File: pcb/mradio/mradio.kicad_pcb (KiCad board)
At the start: 6 copper layers, 132.2 x 75 mm, 191 parts, among them J101 Conn_02x07_Odd_Even, J202 Conn_01x02, J301 2250065-1, J401 MM60-52B1-E1-R650, J501 MDT420E01001, Q101 Q_NMOS, Q102 Q_NMOS, Q103 Q_NMOS, Q104 Q_NMOS, Q105 Q_NMOS, Q106 Q_NMOS, Q107 Q_NMOS, Q108 Q_NMOS, Q301 SSM3K56FS_LF, U1 STM32H745ZITx, U301 DP83825I, U401 74AVC4T774, U402 74AVC4T774, U502 SN74LVC1T45DRL, U601 TPS54560BDDA, U701 TPS54560BDDA, U801 TPS7A8500ARGRR, U901 TPS7A8500ARGRR, Y301 DSC1525JL2A-25M00000T

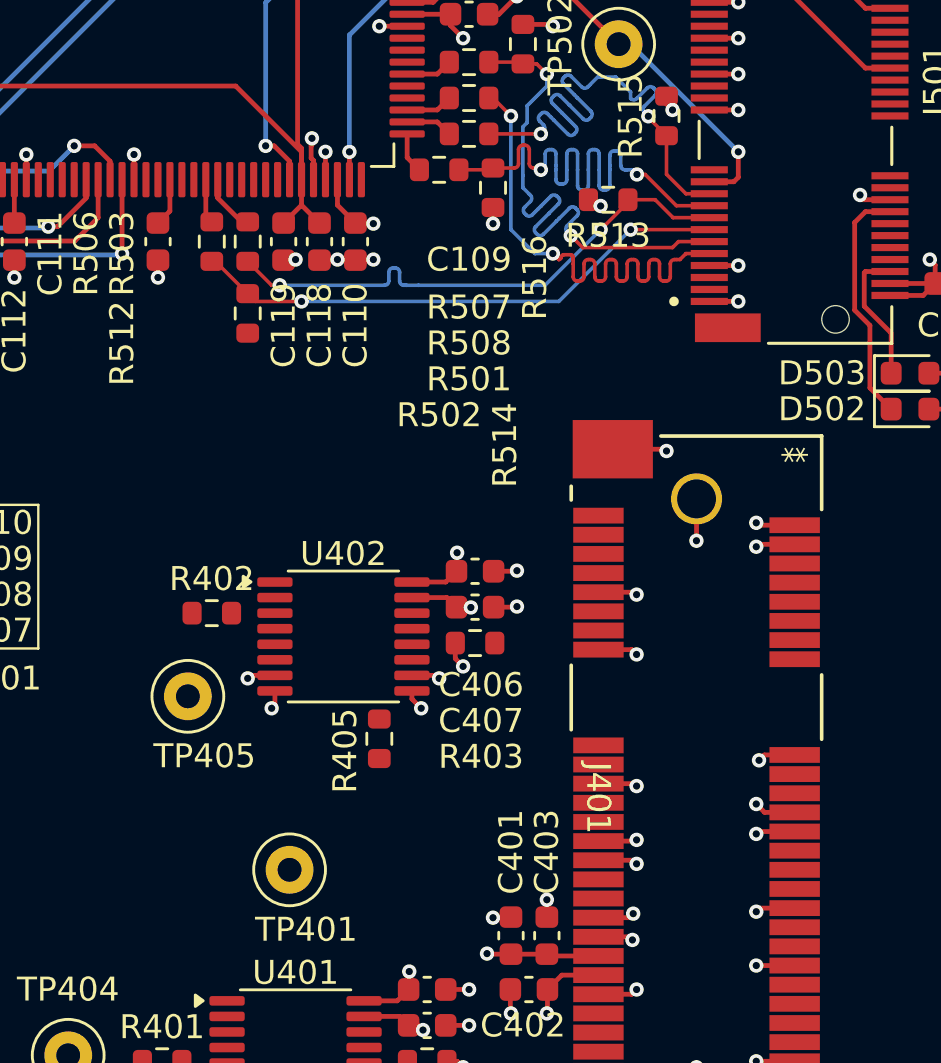
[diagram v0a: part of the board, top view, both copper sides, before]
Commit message: add some more 900 MHz traces
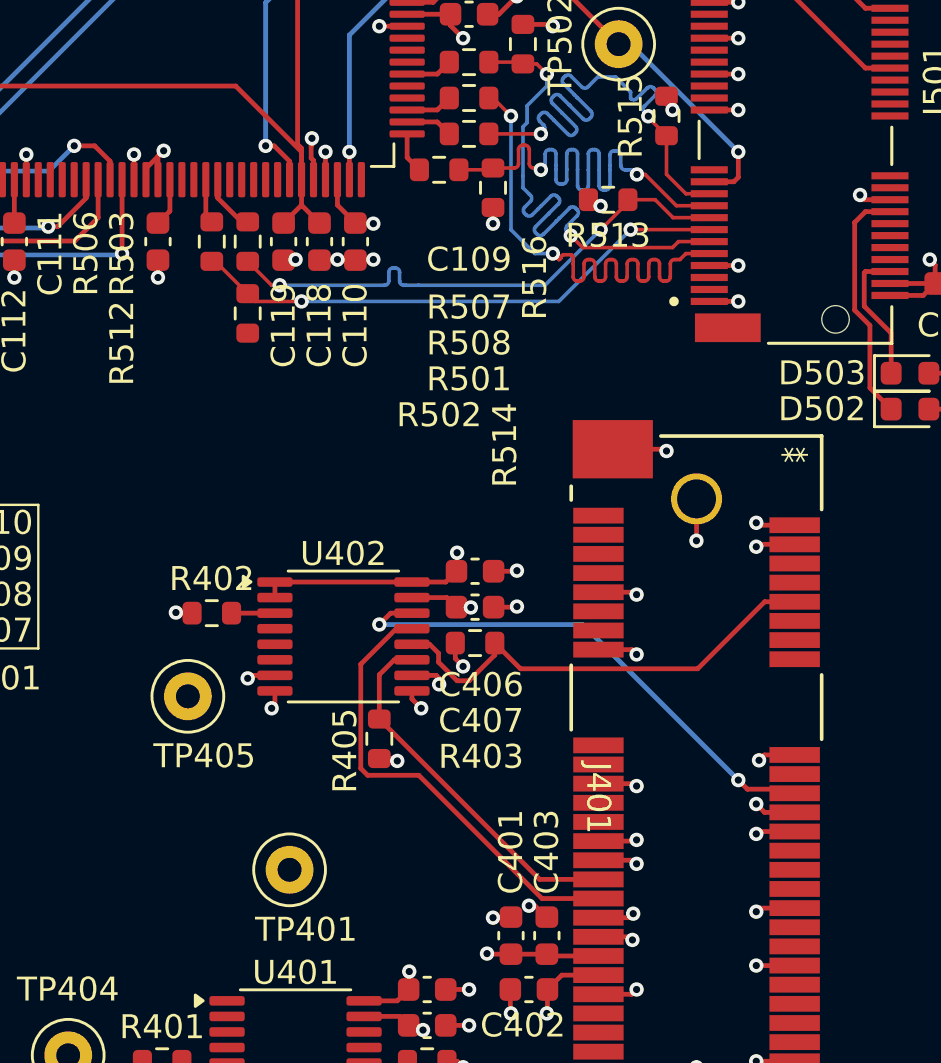
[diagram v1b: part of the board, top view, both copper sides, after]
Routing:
- net /900 Mhz/WM_RESET_3V3: track 0.00 -> 21.8 mm, vias 0 -> 2
- net /900 Mhz/SPI_INT_3V3: track 0.00 -> 19.4 mm
- net /900 Mhz/WM_WAKE_3V3: track 0.00 -> 19.3 mm
- net /900 Mhz/WM_BUSY_3V3: track 0.00 -> 15.4 mm
- net +1V8: track 64.1 -> 71.2 mm, vias 26 -> 27
- net +3V3: track 41.7 -> 44.5 mm, vias 23 -> 24
- net WM_RESET: track 0.00 -> 1.81 mm
- net GND: track 117.4 -> 118.6 mm, vias 99 -> 100

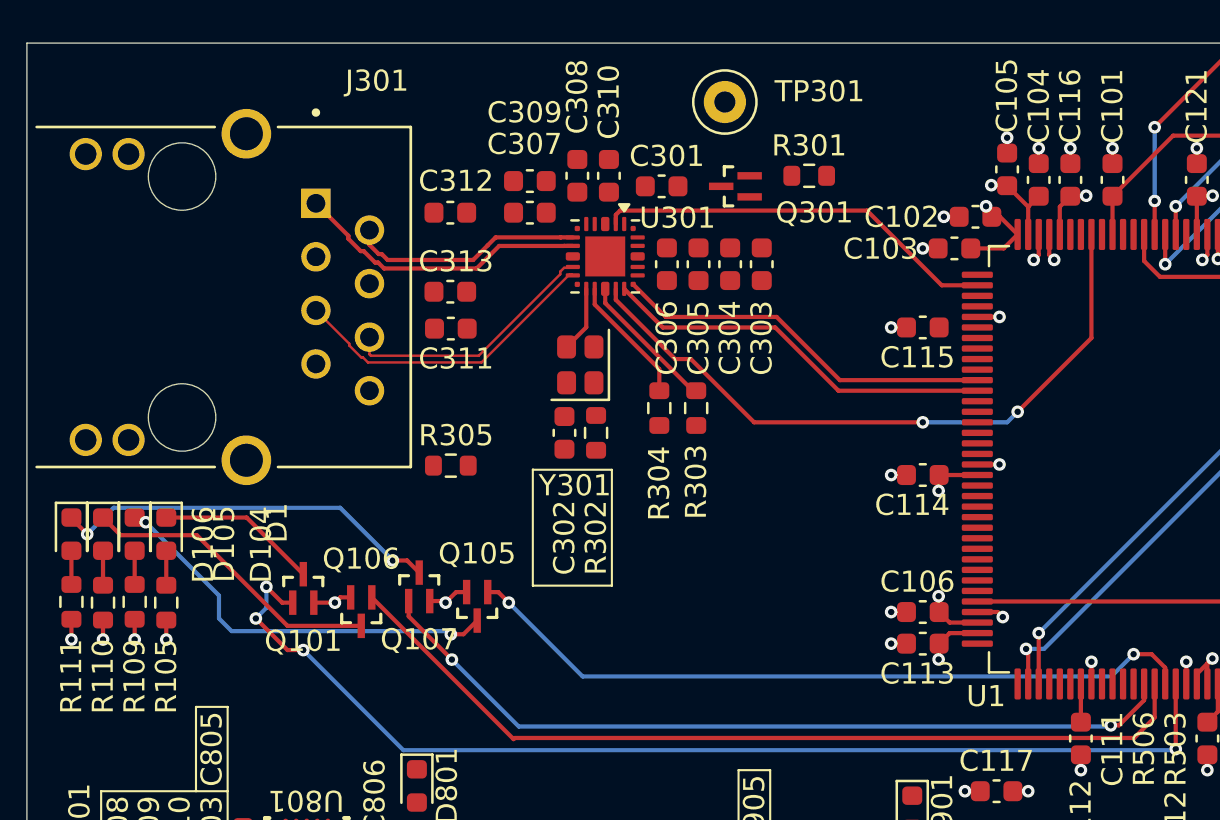
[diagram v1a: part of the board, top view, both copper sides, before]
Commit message: eth routing
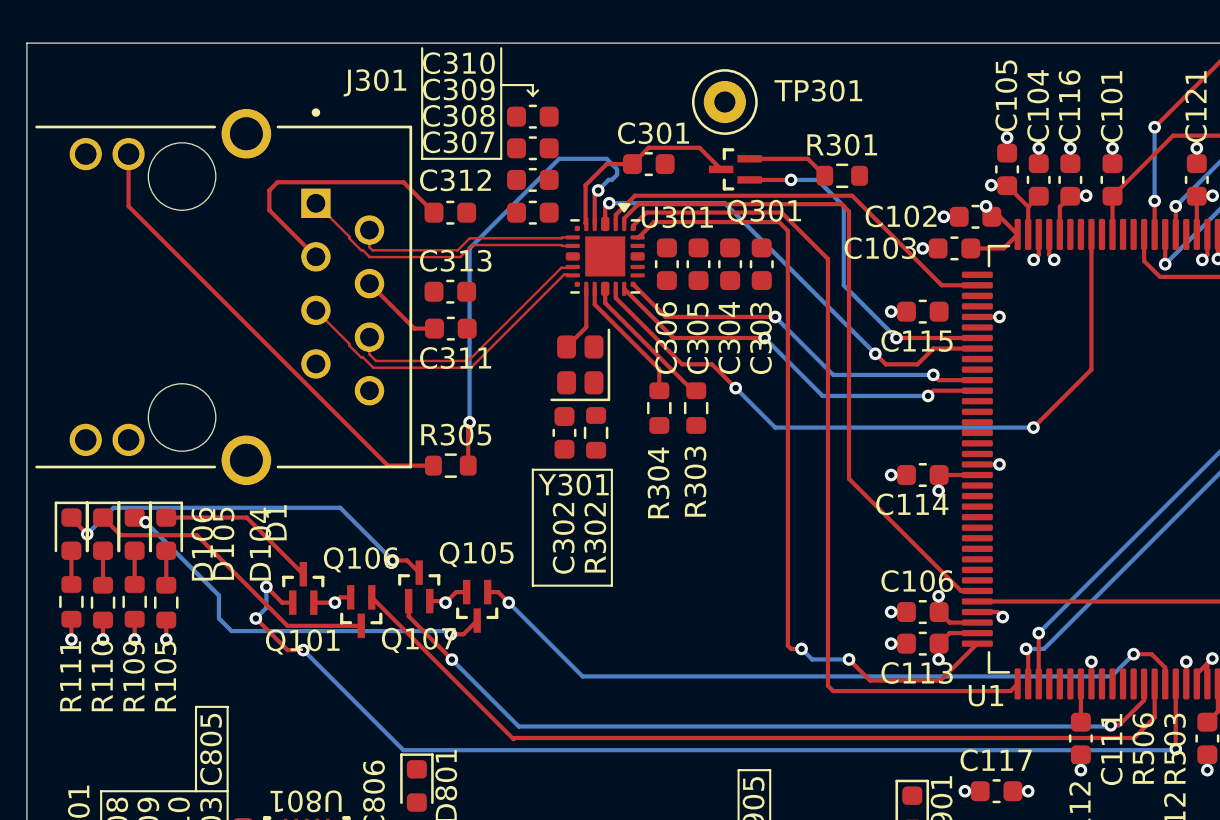
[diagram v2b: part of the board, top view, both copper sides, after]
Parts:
- moved C310 4.57 mm to (79.2, 56.0), turned to 0 degrees
- moved C308 2.12 mm to (79.2, 59.0), turned to 0 degrees
- moved R301 1.56 mm to (93.9, 58.8)
- moved C309 1.56 mm to (79.2, 57.5)
- moved C301 1.22 mm to (84.8, 58.2)
- moved Q301 0.80 mm to (88.9, 58.5)
- moved C115 0.75 mm to (97.8, 65.2)
- moved C307 0.14 mm to (79.2, 60.6)
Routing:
- net ETH_TXD1: track 0.00 -> 40.0 mm
- net ETH_TXD0: track 0.00 -> 37.7 mm, vias 0 -> 2
- net ETH_TX_EN: track 0.00 -> 32.3 mm
- net /Ethernet/ETH_LINK: track 0.00 -> 23.0 mm, vias 0 -> 2
- net ETH_INT: track 0.00 -> 22.2 mm, vias 0 -> 2
- net Net-(J301-Pad9): track 0.00 -> 22.0 mm
- net ETH_RESET: track 0.00 -> 16.1 mm, vias 0 -> 2
- net Net-(J301-RCT): track 0.00 -> 12.6 mm
- net Net-(Q301-D): track 0.00 -> 9.45 mm
- net Net-(J301-TCT): track 0.00 -> 3.97 mm
- net Net-(Q301-S): track 0.00 -> 3.90 mm
- net ETH_MDC: track 32.1 -> 33.1 mm
- net /Ethernet/ETH_RD-: track 11.6 -> 10.8 mm
- net ETH_REF_CLK: track 19.1 -> 19.7 mm
- net ETH_RXD1: track 18.8 -> 19.0 mm, vias 0 -> 2
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
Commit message: eth changes
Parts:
- moved C303 2.44 mm to (92.5, 62.5)
- moved C304 2.44 mm to (91.0, 62.5)
- moved C305 2.44 mm to (89.5, 62.5)
- moved C306 1.34 mm to (86.5, 64.0), turned to 180 degrees
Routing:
- net ETH_TXD1: track 40.0 -> 0.00 mm
- net ETH_TXD0: track 37.7 -> 0.05 mm, vias 2 -> 0
- net ETH_TX_EN: track 32.3 -> 0.00 mm
- net ETH_CRS_DV: track 0.00 -> 18.1 mm
- net +1V8: track 71.2 -> 72.9 mm
- net ETH_RXD1: track 19.0 -> 18.8 mm, vias 2 -> 0
- net ETH_RXD0: vias 2 -> 0

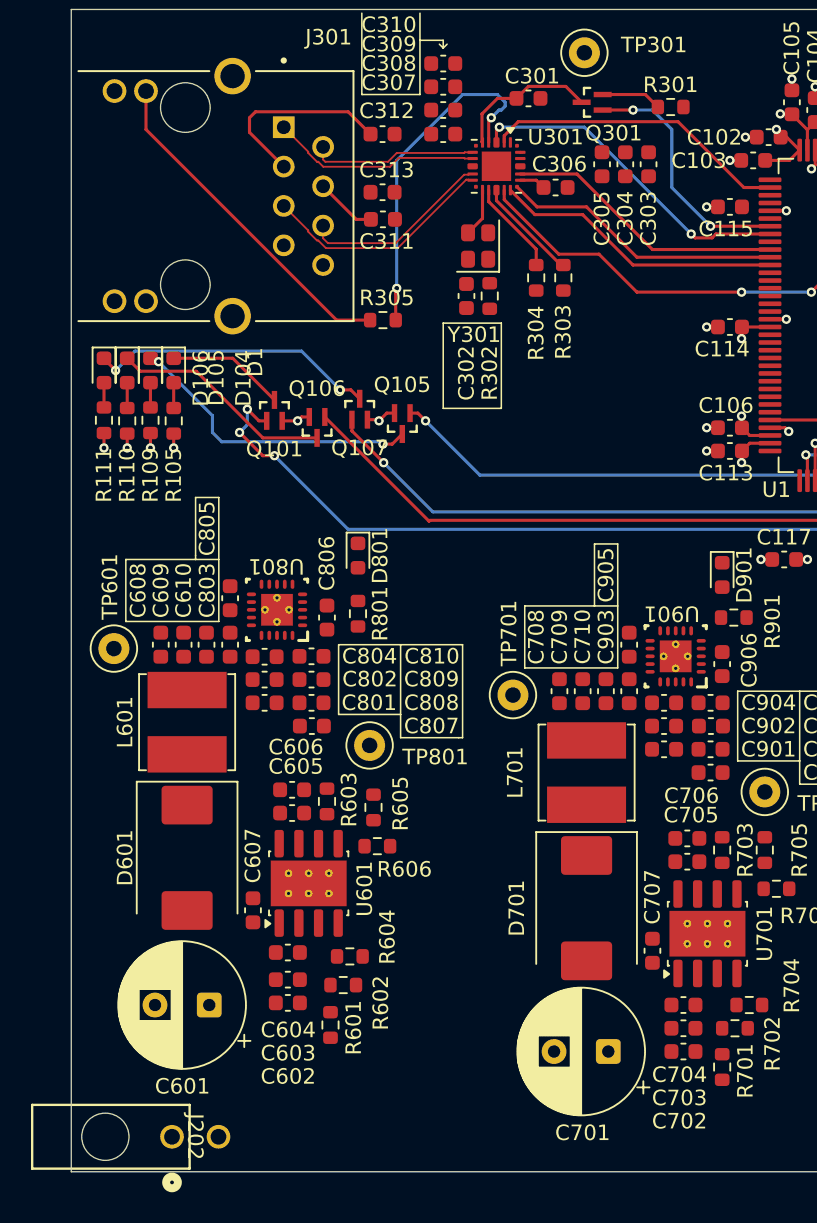
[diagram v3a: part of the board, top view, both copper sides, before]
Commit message: 12v to 3v3 circuit
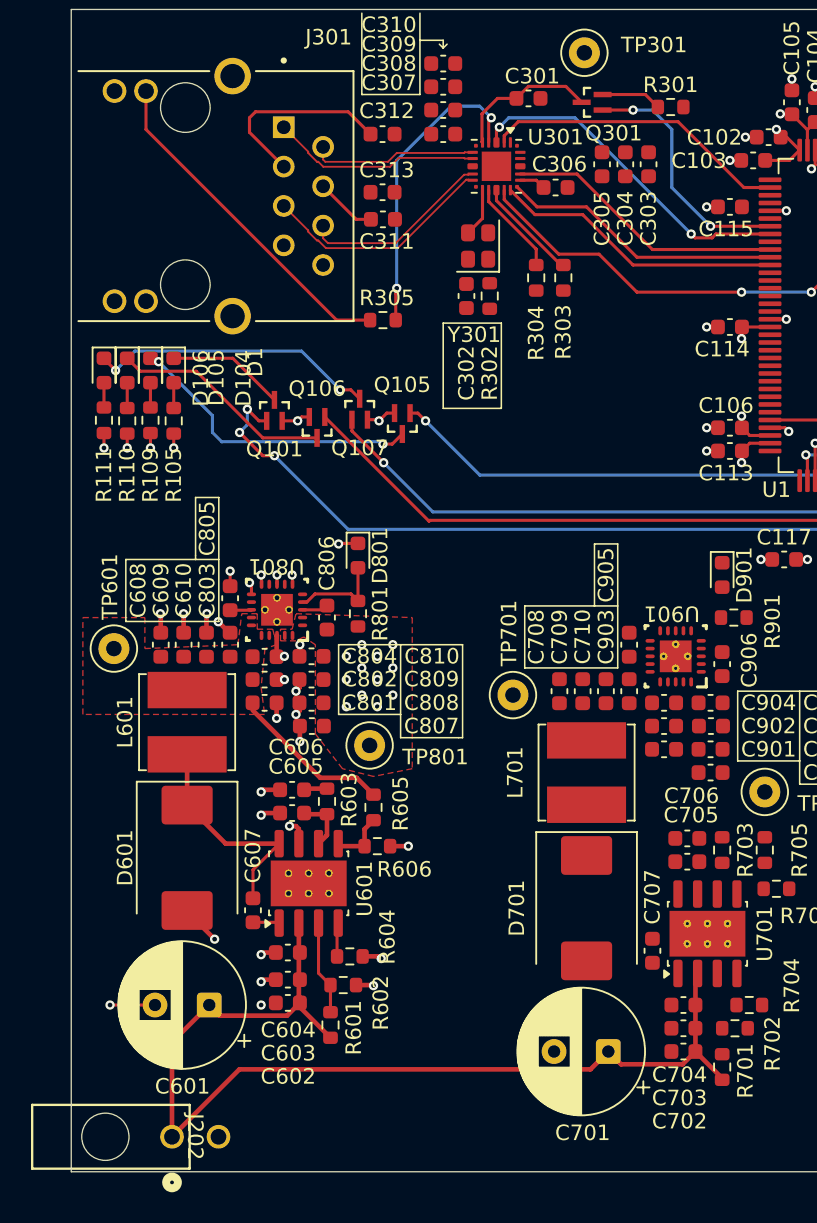
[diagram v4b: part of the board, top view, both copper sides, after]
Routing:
- net +12V: track 0.00 -> 68.6 mm
- net GND: track 118.6 -> 150.5 mm, vias 100 -> 128
- net Net-(D601-K): track 0.00 -> 14.5 mm
- net +3V7: track 0.00 -> 10.5 mm
- net Net-(D801-A): track 0.00 -> 6.12 mm
- net Net-(U601-EN): track 0.00 -> 6.07 mm
- net /Power Distribution/3v7_Buck/FB: track 0.00 -> 3.68 mm
- net Net-(U601-COMP): track 0.00 -> 3.63 mm
- net /Ethernet/ETH_LINK: track 23.0 -> 19.9 mm
- net Net-(U601-RT/CLK): track 0.00 -> 2.18 mm
- net Net-(U601-BOOT): track 0.00 -> 1.71 mm
- net Net-(U801-FB): track 0.00 -> 1.69 mm
- net Net-(C606-Pad1): track 0.00 -> 1.51 mm
- net Net-(U801-NR_SS): track 0.00 -> 1.39 mm
- net ETH_INT: track 21.8 -> 22.3 mm
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- added copper zone on F.Cu, net +3V3
- added copper zone on F.Cu, net +3V7

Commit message: Changed 2v2 testpoint net to actually be 2v2...
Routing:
- net Net-(D701-K): track 0.00 -> 13.8 mm
- net GND: track 150.5 -> 162.2 mm, vias 128 -> 138
- net +2V2: track 0.00 -> 9.63 mm, vias 0 -> 1
- net Net-(U701-EN): track 0.00 -> 5.34 mm
- net Net-(U701-COMP): track 0.00 -> 3.65 mm
- net /Power Distribution/2v2_Buck/FB: track 0.00 -> 3.57 mm
- net Net-(U701-RT/CLK): track 0.00 -> 2.05 mm
- net Net-(U701-BOOT): track 0.00 -> 1.93 mm
- net Net-(C706-Pad1): track 0.00 -> 1.51 mm

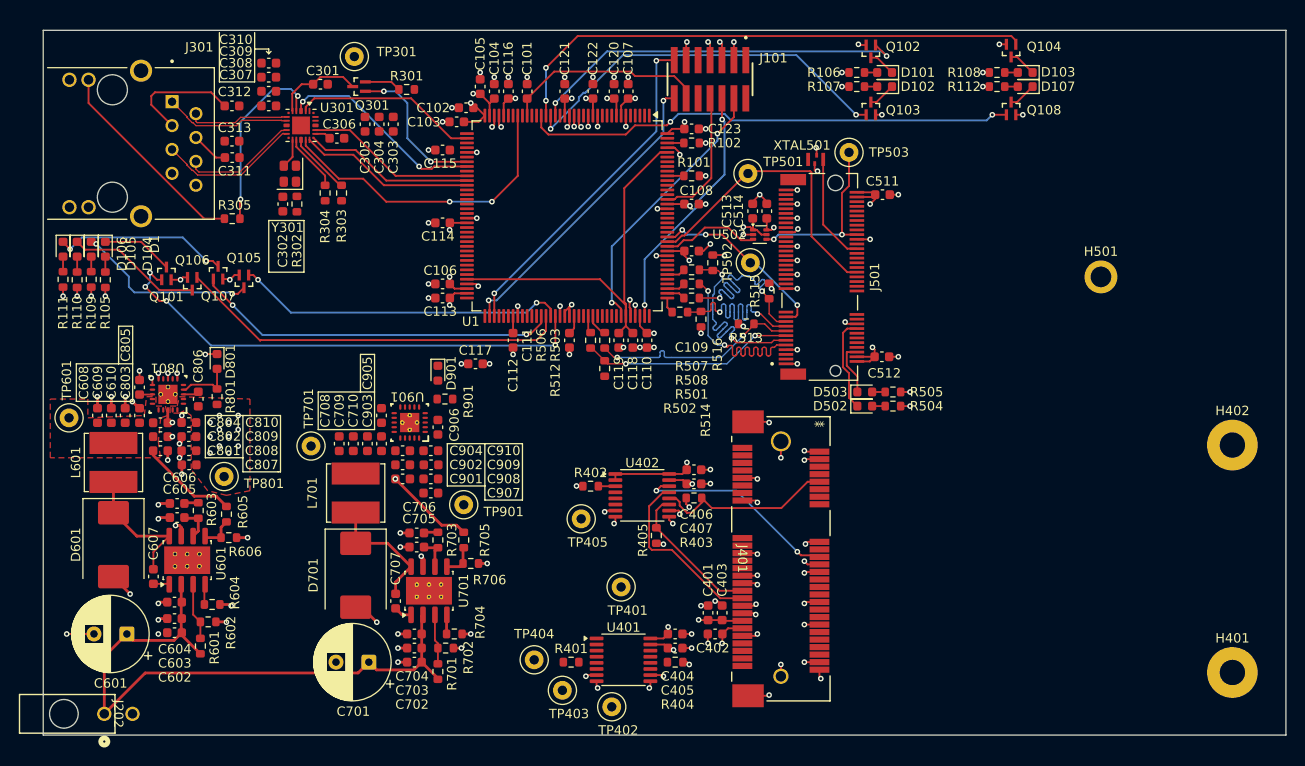
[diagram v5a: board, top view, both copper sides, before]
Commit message: all traces routed
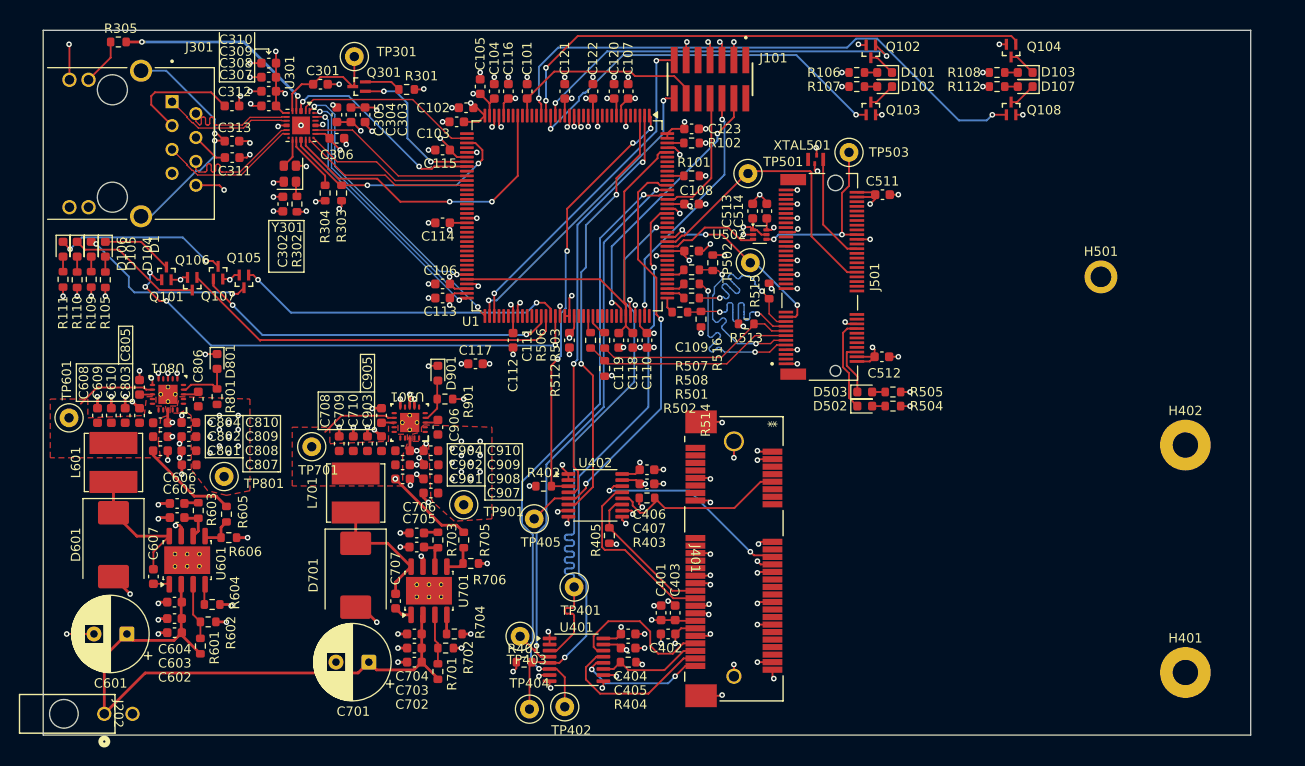
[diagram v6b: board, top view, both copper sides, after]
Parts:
- moved R305 22.4 mm to (63.2, 53.8)
- moved TP403 7.30 mm to (106.0, 117.0)
- moved TP404 5.27 mm to (107.0, 124.8)
- moved C401 5.00 mm to (121.0, 114.5)
- moved C402 5.00 mm to (121.8, 116.8)
- moved C403 5.00 mm to (122.5, 114.5)
- moved C404 5.00 mm to (117.5, 116.8)
- moved C405 5.00 mm to (117.5, 118.2)
- moved C406 5.00 mm to (119.5, 99.3)
- moved C407 5.00 mm to (119.5, 100.8)
- moved H401 5.00 mm to (176.8, 120.8)
- moved H402 5.00 mm to (176.8, 96.7)
- moved J401 5.00 mm to (128.8, 108.8)
- moved R401 5.00 mm to (106.4, 119.8)
- moved R402 5.00 mm to (108.5, 101.0)
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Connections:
- TP701 pad 1: Net-(D701-K) -> +2V2
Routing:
- net SPI1_MISO: track 0.00 -> 65.6 mm, vias 0 -> 2
- net SPI1_CS: track 0.00 -> 62.0 mm, vias 0 -> 2
- net SPI1_SCK: track 0.00 -> 60.0 mm, vias 0 -> 1
- net SPI1_MOSI: track 0.00 -> 59.6 mm, vias 0 -> 2
- net SPI_INT: track 0.00 -> 46.3 mm, vias 0 -> 2
- net WM_BUSY: track 0.00 -> 46.0 mm, vias 0 -> 2
- net GND: track 162.2 -> 207.6 mm, vias 138 -> 174
- net WM_WAKE: track 0.00 -> 44.4 mm, vias 0 -> 2
- net WM_RESET: track 1.81 -> 45.9 mm, vias 0 -> 4
- net ETH_TXD1: track 0.00 -> 30.7 mm, vias 0 -> 2
- net ETH_TX_EN: track 0.00 -> 27.7 mm, vias 0 -> 2
- net ETH_TXD0: track 0.00 -> 27.3 mm, vias 0 -> 2
- net Net-(J301-SHIELD): track 0.00 -> 26.1 mm, vias 0 -> 2
- net ETH_MDIO: track 6.71 -> 25.8 mm, vias 0 -> 2
- net /900 Mhz/SPI1_MOSI_3V3: track 0.00 -> 17.5 mm
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- added copper zone on F.Cu, net +1V8
- added copper zone on F.Cu, net +2V2
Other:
- board size 132.2 x 75 mm -> 128.5 x 75 mm
